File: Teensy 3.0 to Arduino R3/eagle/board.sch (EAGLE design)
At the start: 28 parts, among them IC1 7805TV

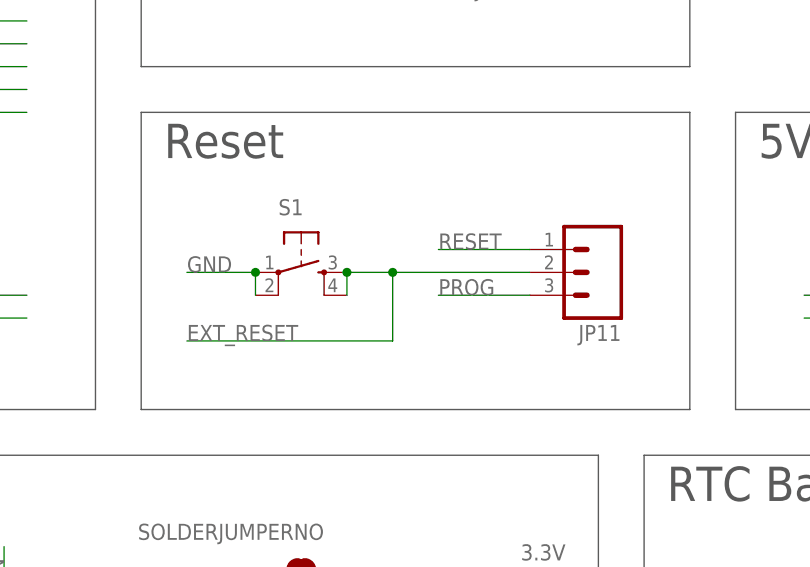
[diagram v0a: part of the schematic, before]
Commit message: update Arduino R3 board
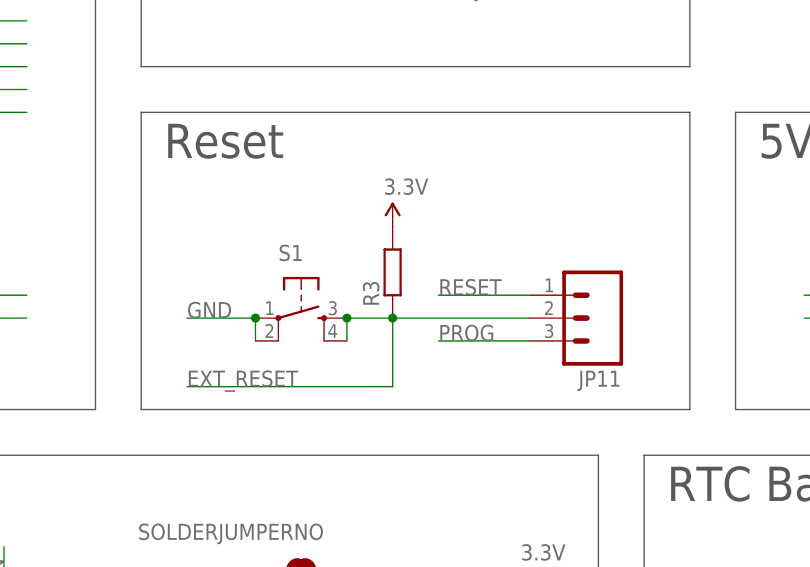
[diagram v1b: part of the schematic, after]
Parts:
- added R3: (no value), rcl:R-EU_R0805
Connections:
- net 3V3: now also R3.2
- net EXT_RESET: now also R3.1
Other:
- moved on the sheet: JP11, S1
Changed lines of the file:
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@@
 <part name="JP13" library="adafruit" deviceset="PINHD-1X13" device="_BIG"/>
 <part name="JP14" library="SparkFun-Connectors" deviceset="M02" device="PTH"/>
+<part name="R3" library="rcl" deviceset="R-EU_" device="R0805"/>
+<part name="P+3" library="SparkFun-Aesthetics" deviceset="3.3V" device=""/>
 </parts>
 <sheets>
@@
 <instance part="P+4" gate="G$1" x="203.2" y="60.96"/>
 <instance part="JP10" gate="G$1" x="147.32" y="40.64" rot="R90"/>
-<instance part="S1" gate="S" x="177.8" y="96.52"/>
+<instance part="S1" gate="S" x="177.8" y="91.44"/>
 <instance part="BAT1" gate="G$1" x="238.76" y="48.26"/>
-<instance part="JP11" gate="G$1" x="210.82" y="96.52" rot="R180"/>
+<instance part="JP11" gate="G$1" x="210.82" y="91.44" rot="R180"/>
 <instance part="JP12" gate="A" x="185.42" y="147.32"/>
 <instance part="JP13" gate="A" x="195.58" y="147.32" rot="R180"/>
 <instance part="JP14" gate="G$1" x="251.46" y="93.98" rot="R180"/>
+<instance part="R3" gate="G$1" x="187.96" y="96.52" rot="R90"/>
+<instance part="P+3" gate="G$1" x="187.96" y="101.6"/>
 </instances>
 <busses>
@@
 </segment>
 <segment>
-<wire x1="172.72" y1="96.52" x2="172.72" y2="93.98" width="0.1524" layer="91"/>
-<wire x1="172.72" y1="96.52" x2="165.1" y2="96.52" width="0.1524" layer="91"/>
-<label x="165.1" y="96.52" size="1.778" layer="95"/>
+<wire x1="172.72" y1="91.44" x2="172.72" y2="88.9" width="0.1524" layer="91"/>
+<wire x1="172.72" y1="91.44" x2="165.1" y2="91.44" width="0.1524" layer="91"/>
+<label x="165.1" y="91.44" size="1.778" layer="95"/>
 <pinref part="S1" gate="S" pin="1"/>
-<junction x="172.72" y="96.52"/>
+<junction x="172.72" y="91.44"/>
 <pinref part="S1" gate="S" pin="2"/>
 </segment>
@@
 <label x="236.22" y="93.98" size="1.778" layer="95"/>
 </segment>
+<segment>
+<pinref part="R3" gate="G$1" pin="2"/>
+<pinref part="P+3" gate="G$1" pin="3.3V"/>
+</segment>
 </net>
 <net name="A9" class="0">
@@
 <segment>
 <pinref part="JP11" gate="G$1" pin="3"/>
-<wire x1="203.2" y1="93.98" x2="193.04" y2="93.98" width="0.1524" layer="91"/>
-<label x="193.04" y="93.98" size="1.778" layer="95"/>
+<wire x1="203.2" y1="88.9" x2="193.04" y2="88.9" width="0.1524" layer="91"/>
+<label x="193.04" y="88.9" size="1.778" layer="95"/>
 </segment>
 </net>
@@
 <segment>
 <pinref part="JP11" gate="G$1" pin="1"/>
-<wire x1="203.2" y1="99.06" x2="193.04" y2="99.06" width="0.1524" layer="91"/>
-<label x="193.04" y="99.06" size="1.778" layer="95"/>
+<wire x1="203.2" y1="93.98" x2="193.04" y2="93.98" width="0.1524" layer="91"/>
+<label x="193.04" y="93.98" size="1.778" layer="95"/>
 </segment>
 </net>
@@
 </segment>
 <segment>
-<wire x1="182.88" y1="96.52" x2="182.88" y2="93.98" width="0.1524" layer="91"/>
-<wire x1="182.88" y1="96.52" x2="187.96" y2="96.52" width="0.1524" layer="91"/>
+<wire x1="182.88" y1="91.44" x2="182.88" y2="88.9" width="0.1524" layer="91"/>
+<wire x1="182.88" y1="91.44" x2="187.96" y2="91.44" width="0.1524" layer="91"/>
 <pinref part="S1" gate="S" pin="3"/>
-<junction x="182.88" y="96.52"/>
+<junction x="182.88" y="91.44"/>
 <pinref part="S1" gate="S" pin="4"/>
 <pinref part="JP11" gate="G$1" pin="2"/>
-<wire x1="187.96" y1="96.52" x2="203.2" y2="96.52" width="0.1524" layer="91"/>
-<wire x1="165.1" y1="88.9" x2="187.96" y2="88.9" width="0.1524" layer="91"/>
-<wire x1="187.96" y1="88.9" x2="187.96" y2="96.52" width="0.1524" layer="91"/>
-<junction x="187.96" y="96.52"/>
-<label x="165.1" y="88.9" size="1.778" layer="95"/>
-</segment>
-</net>
+<wire x1="187.96" y1="91.44" x2="203.2" y2="91.44" width="0.1524" layer="91"/>
+<wire x1="165.1" y1="83.82" x2="187.96" y2="83.82" width="0.1524" layer="91"/>
+<wire x1="187.96" y1="83.82" x2="187.96" y2="91.44" width="0.1524" layer="91"/>
+<junction x="187.96" y="91.44"/>
+<label x="165.1" y="83.82" size="1.778" layer="95"/>
+<pinref part="R3" gate="G$1" pin="1"/>
+</segment>
+</net>

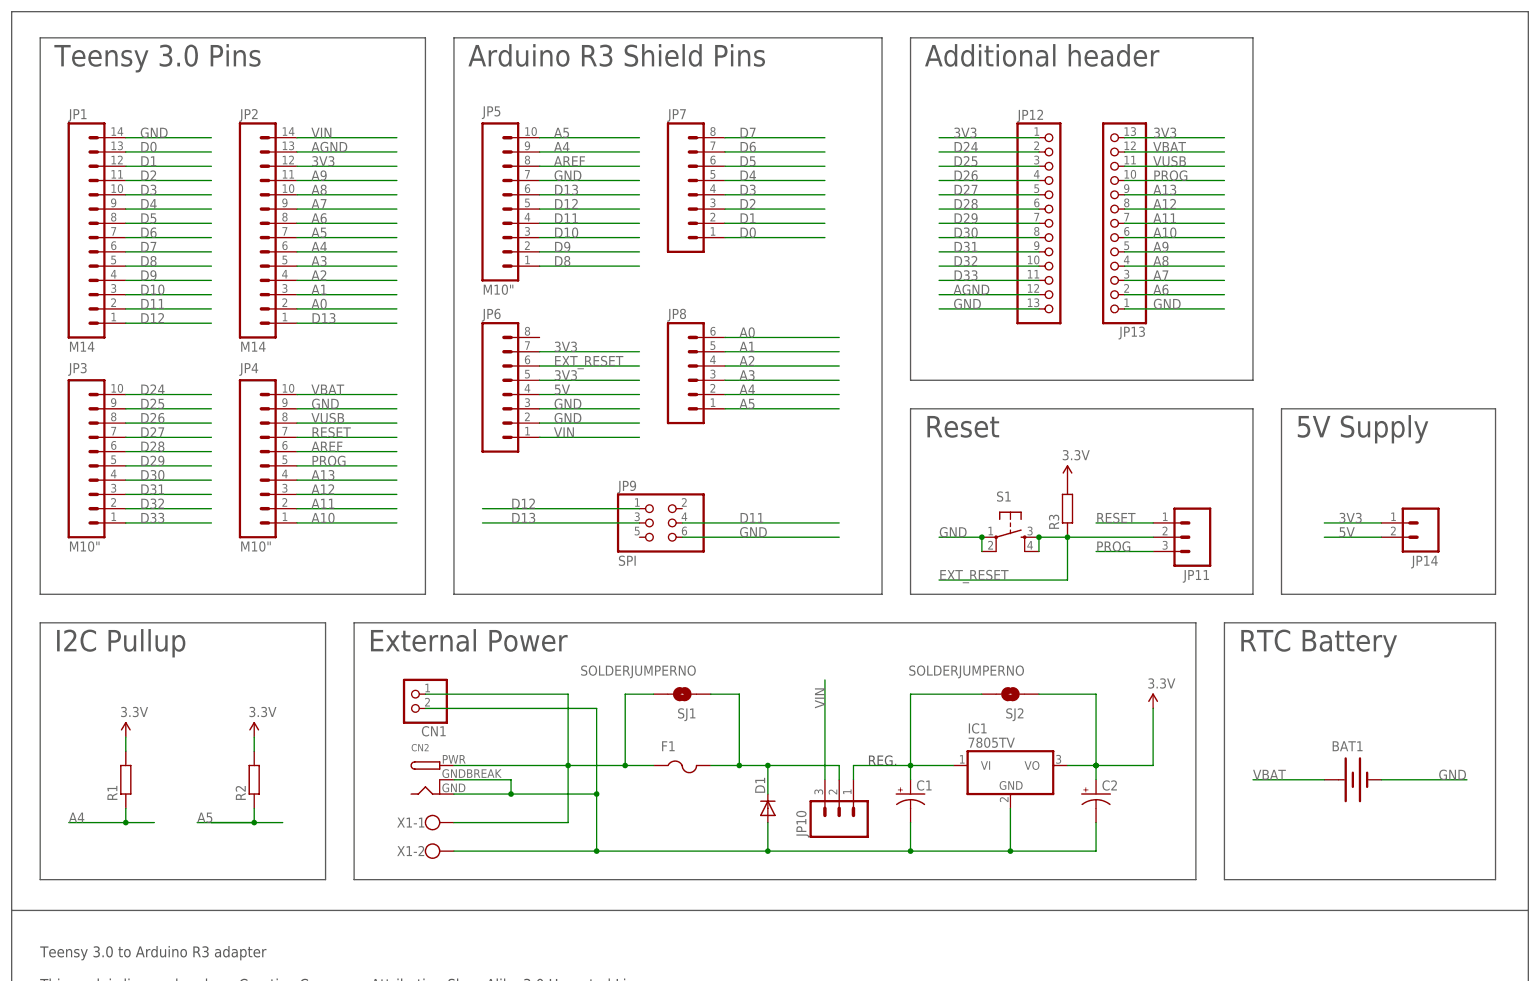
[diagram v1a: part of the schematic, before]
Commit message: update: -Arduino R3 pcb - breadboard pcb
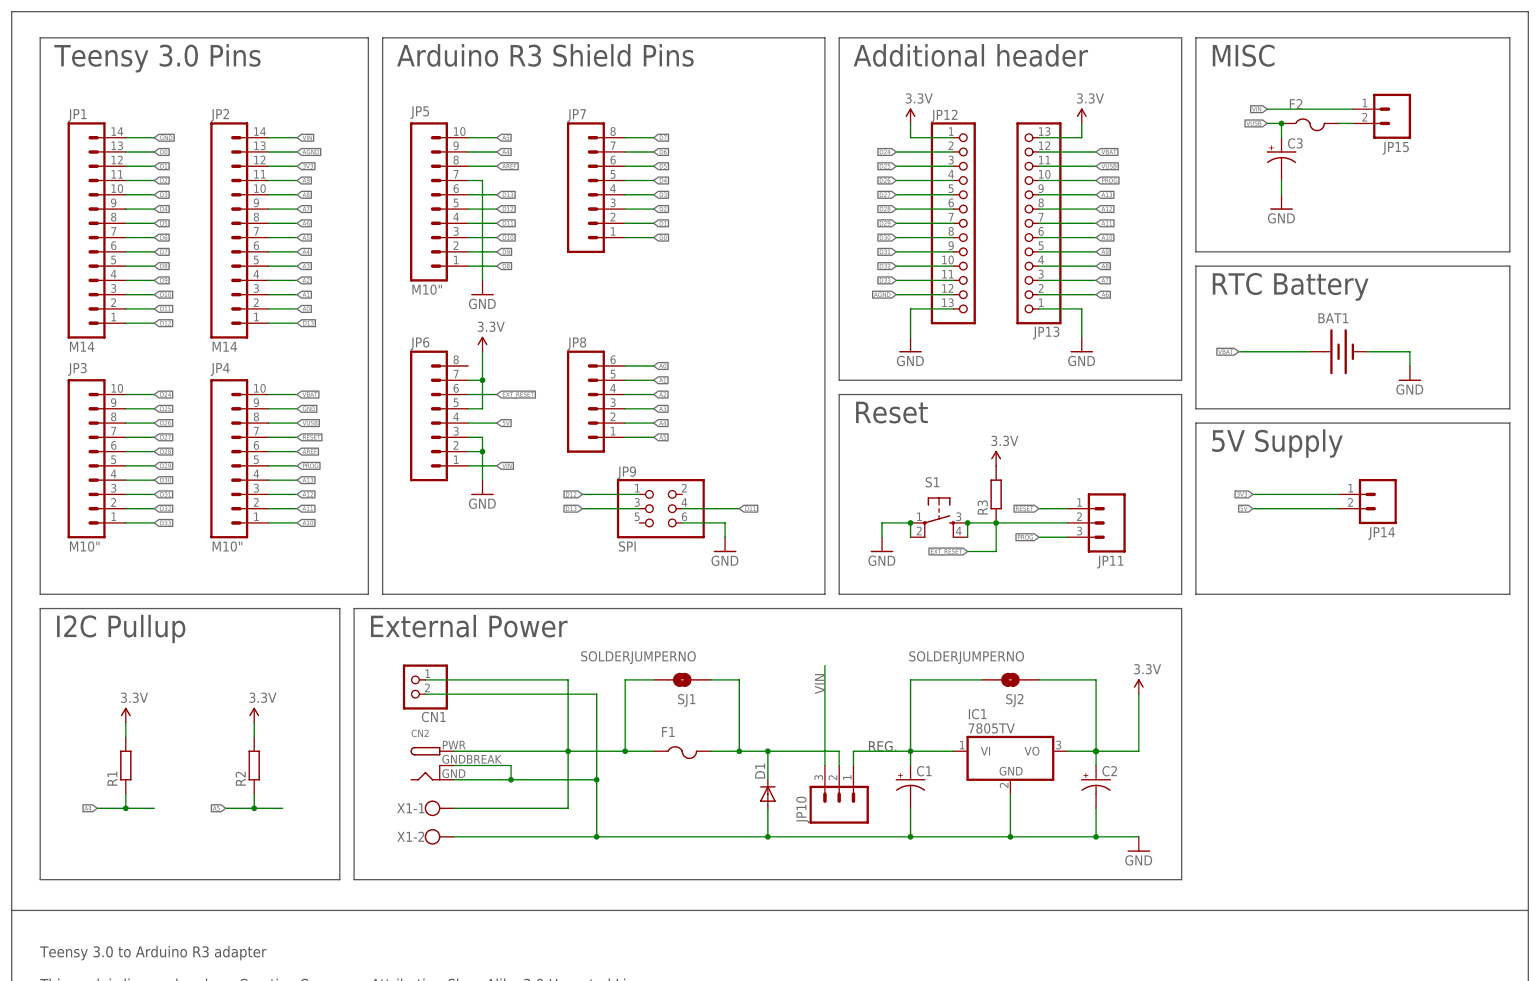
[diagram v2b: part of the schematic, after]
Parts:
- added C3: (no value), SparkFun-Capacitors:CAP_POL3528-KIT
- added F2: (no value), adafruit:PTCFUSE-1812
- added JP15: (no value), SparkFun-Connectors:M02PTH
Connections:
- new net N$2: F2.2, JP15.2
- net GND: now also C3.-
- net VIN: now also JP15.1
- net VUSB: now also C3.+, F2.1
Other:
- note added: "MISC"
- moved on the sheet: BAT1, C1, C2, CN1, CN2, D1, F1, IC1, JP10, JP11, JP12, JP13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

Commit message: added i2c eeprom, sdcard
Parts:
- added C4, C5, C6, C7, C8: (no value), rcl:C-EUC0805K
- added IC2, IC3, IC4, IC5: 24AA256SN, microchip:24AA256SN
- added R4: (no value), resistor:R-EU_R0805
- added U1: MICROSD, adafruit:MICROSD
- BAT1: device SparkFun-Electromechanical:BATTERY12PTH -> SparkFun-Electromechanical:BATTERY12MM
- C1, C2: device SparkFun-Capacitors:CAP_POL3528-KIT -> resistor:CPOL-EUCT3216
- R1, R2, R3: device rcl:R-EU_R0805 -> resistor:R-EU_R0805
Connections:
- new net 3.3V: JP2.12
- net 3V3: now also C4.1, C5.1, C6.1, C7.1, C8.1, IC2.A2, IC2.VCC, IC3.A1, IC3.A2, IC3.VCC, IC4.A0, IC4.A2, IC4.VCC, IC5.A0, IC5.A1, IC5.A2, IC5.VCC, R4.2, U1.VDD; no longer JP2.12
- net A4: now also IC2.SDA, IC3.SDA, IC4.SDA, IC5.SDA
- net A5: now also IC2.SCL, IC3.SCL, IC4.SCL, IC5.SCL
- net D10: now also U1.CS
- net D11: now also U1.DATA_IN
- net D12: now also U1.DATA_OUT
- net D13: now also U1.SCLK
- net D8: now also R4.1, U1.CARD_DETECT
- net GND: now also C4.2, C5.2, C6.2, C7.2, C8.2, IC2.A0, IC2.A1, IC2.GND, IC2.WP, IC3.A0, IC3.GND, IC3.WP, IC4.A1, IC4.GND, IC4.WP, IC5.GND, IC5.WP, U1.GND, U1.GND1, U1.VSS
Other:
- note added: "I2C EEPROM"
- note added: "uSD socket"
- moved on the sheet: JP3, JP4

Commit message: Version 3 final
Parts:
- added C9: (no value), resistor:CPOL-EUD
- added D2: (no value), SparkFun-DiscreteSemi:DIODESMA-KIT
- added R10, R11, R12, R13, R14, R15, R16, R17, R18, R19, R20, R21, R22, R23, R24, R5, R6, R7, R8, R9: (no value), resistor:R-EU_R0805
- added SJ3, SJ4, SJ5, SJ6: SOLDERJUMPERNO, SparkFun-Passives:SOLDERJUMPERNO
- IC1: value 7805TV -> 78XX compatible
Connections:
- removed net 3V3: C2.+, C4.1, C5.1, C6.1, C7.1, C8.1, IC1.VO, IC2.A2, IC2.VCC, IC3.A1, IC3.A2, IC3.VCC, IC4.A0, IC4.A2, IC4.VCC, IC5.A0, IC5.A1, IC5.A2, IC5.VCC, JP12.1, JP13.13, JP14.1, JP6.5, JP6.7, R1.2, R2.2, R3.2, R4.2, SJ2.1, U1.VDD
- new net N$10: JP2.7, R10.2
- new net N$11: JP2.6, R11.2
- new net N$12: JP2.5, R12.2
- new net N$13: JP1.13, R13.2
- new net N$14: JP1.12, R14.2
- new net N$15: JP1.11, R15.2
- new net N$16: JP1.10, R16.2
- new net N$17: JP1.9, R17.2
- new net N$18: JP1.8, R18.2
- new net N$19: JP1.7, R19.2
- new net N$20: JP1.6, R20.2
- new net N$21: JP2.4, R21.2
- new net N$22: JP2.3, R22.2
- new net N$23: JP2.2, R23.2
- new net N$24: JP2.1, R24.2
- new net N$5: JP1.5, R5.2
- new net N$6: JP1.4, R6.2
- new net N$7: JP1.3, R7.2
- new net N$8: JP1.2, R8.2
- new net N$9: JP1.1, R9.2
- new net NIC: R4.1, SJ3.1, SJ4.1, U1.CARD_DETECT
- new net QW: SJ5.1, SJ6.1, U1.CS
- net 3.3V: now also C2.+, C4.1, C5.1, C6.1, C7.1, C8.1, C9.+, D2.A, IC1.VO, IC2.A2, IC2.VCC, IC3.A1, IC3.A2, IC3.VCC, IC4.A0, IC4.A2, IC4.VCC, IC5.A0, IC5.A1, IC5.A2, IC5.VCC, JP12.1, JP13.13, JP14.1, JP6.5, JP6.7, R1.2, R2.2, R3.2, R4.2, SJ2.1, U1.VDD
- net A0: now also R23.1; no longer JP2.2
- net A1: now also R22.1; no longer JP2.3
- net A2: now also R21.1; no longer JP2.4
- net A3: now also R12.1; no longer JP2.5
- net A4: now also R11.1; no longer JP2.6
- net A5: now also R10.1; no longer JP2.7
- net D0: now also R13.1; no longer JP1.13
- net D1: now also R14.1; no longer JP1.12
- net D10: now also R7.1, SJ6.2; no longer JP1.3, U1.CS
- net D11: now also R8.1; no longer JP1.2
- net D12: now also R9.1; no longer JP1.1
- net D13: now also R24.1; no longer JP2.1
- net D2: now also R15.1; no longer JP1.11
- net D3: now also R16.1; no longer JP1.10
- net D4: now also R17.1; no longer JP1.9
- net D5: now also R18.1; no longer JP1.8
- net D6: now also R19.1; no longer JP1.7
- net D7: now also R20.1, SJ3.2; no longer JP1.6
- net D8: now also R5.1, SJ4.2; no longer JP1.5, R4.1, U1.CARD_DETECT
- net D9: now also R6.1, SJ5.2; no longer JP1.4
- net GND: now also C9.-
- net N$3: now also D2.C
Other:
- moved on the sheet: BAT1, C3, C4, F2, JP1, JP11, JP12, JP13, JP14, JP15, JP2, JP3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

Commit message: V3-2: fixed several bugs
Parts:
- added C10: (no value), rcl:CPOL-EUSANYO_SMD_E7
- added JP16: (no value), SparkFun-Connectors:M02PTH
- C3: device SparkFun-Capacitors:CAP_POL3528-KIT -> rcl:CPOL-EUA/3216-18W
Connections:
- new net N$25: C10.+, JP16.2
- net GND: now also C10.-
- net N$2: now also JP16.1
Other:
- moved on the sheet: C3, F2, JP15
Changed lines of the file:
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@@
 <part name="F2" library="adafruit" deviceset="PTCFUSE" device="-1812"/>
 <part name="JP15" library="SparkFun-Connectors" deviceset="M02" device="PTH"/>
-<part name="C3" library="SparkFun-Capacitors" deviceset="CAP_POL" device="3528-KIT"/>
+<part name="C3" library="rcl" deviceset="CPOL-EU" device="A/3216-18W"/>
 <part name="GND1" library="SparkFun-Aesthetics" deviceset="GND" device=""/>
 <part name="GND2" library="SparkFun-Aesthetics" deviceset="GND" device=""/>
@@
 <part name="R23" library="resistor" deviceset="R-EU_" device="R0805"/>
 <part name="R24" library="resistor" deviceset="R-EU_" device="R0805"/>
+<part name="GND22" library="SparkFun-Aesthetics" deviceset="GND" device=""/>
+<part name="JP16" library="SparkFun-Connectors" deviceset="M02" device="PTH"/>
+<part name="C10" library="rcl" deviceset="CPOL-EU" device="SANYO_SMD_E7"/>
 </parts>
 <sheets>
@@
 <instance part="R3" gate="G$1" x="198.12" y="99.06" rot="R90"/>
 <instance part="P+3" gate="G$1" x="198.12" y="104.14"/>
-<instance part="F2" gate="G$1" x="393.7" y="99.06"/>
-<instance part="JP15" gate="G$1" x="408.94" y="104.14" rot="R180"/>
-<instance part="C3" gate="G$1" x="388.62" y="96.52"/>
-<instance part="GND1" gate="1" x="388.62" y="86.36"/>
+<instance part="F2" gate="G$1" x="391.16" y="102.87"/>
+<instance part="JP15" gate="G$1" x="415.29" y="107.95" rot="R180"/>
+<instance part="C3" gate="G$1" x="386.08" y="97.79"/>
+<instance part="GND1" gate="1" x="386.08" y="82.55"/>
 <instance part="GND2" gate="1" x="106.68" y="99.06"/>
 <instance part="GND3" gate="1" x="149.86" y="88.9"/>
@@
 <attribute name="VALUE" x="72.39" y="134.112" size="1.778" layer="96" rot="R180"/>
 </instance>
+<instance part="GND22" gate="1" x="401.32" y="82.55"/>
+<instance part="JP16" gate="G$1" x="415.29" y="95.25" rot="R180"/>
+<instance part="C10" gate="G$1" x="401.32" y="90.17"/>
 </instances>
 <busses>
@@
 <pinref part="C3" gate="G$1" pin="-"/>
 <pinref part="GND1" gate="1" pin="GND"/>
-<wire x1="388.62" y1="91.44" x2="388.62" y2="88.9" width="0.1524" layer="91"/>
+<wire x1="386.08" y1="92.71" x2="386.08" y2="85.09" width="0.1524" layer="91"/>
 </segment>
 <segment>
@@
 <wire x1="457.2" y1="147.32" x2="459.74" y2="147.32" width="0.1524" layer="91"/>
 </segment>
+<segment>
+<pinref part="GND22" gate="1" pin="GND"/>
+<pinref part="C10" gate="G$1" pin="-"/>
+</segment>
 </net>
 <net name="D0" class="0">
@@
 <segment>
 <pinref part="JP15" gate="G$1" pin="1"/>
-<wire x1="401.32" y1="104.14" x2="386.08" y2="104.14" width="0.1524" layer="91"/>
-<label x="386.08" y="104.14" size="0.8128" layer="95" rot="R180" xref="yes"/>
+<wire x1="407.67" y1="107.95" x2="383.54" y2="107.95" width="0.1524" layer="91"/>
+<label x="383.54" y="107.95" size="0.8128" layer="95" rot="R180" xref="yes"/>
 </segment>
 </net>
@@
 <segment>
 <pinref part="F2" gate="G$1" pin="1"/>
-<wire x1="388.62" y1="101.6" x2="386.08" y2="101.6" width="0.1524" layer="91"/>
-<label x="386.08" y="101.6" size="0.8128" layer="95" rot="R180" xref="yes"/>
+<wire x1="386.08" y1="105.41" x2="383.54" y2="105.41" width="0.1524" layer="91"/>
+<label x="383.54" y="105.41" size="0.8128" layer="95" rot="R180" xref="yes"/>
 <pinref part="C3" gate="G$1" pin="+"/>
-<wire x1="388.62" y1="99.06" x2="388.62" y2="101.6" width="0.1524" layer="91"/>
-<junction x="388.62" y="101.6"/>
+<wire x1="386.08" y1="100.33" x2="386.08" y2="105.41" width="0.1524" layer="91"/>
+<junction x="386.08" y="105.41"/>
 </segment>
 </net>
@@
 <pinref part="F2" gate="G$1" pin="2"/>
 <pinref part="JP15" gate="G$1" pin="2"/>
-<wire x1="398.78" y1="101.6" x2="401.32" y2="101.6" width="0.1524" layer="91"/>
+<wire x1="396.24" y1="105.41" x2="401.32" y2="105.41" width="0.1524" layer="91"/>
+<pinref part="JP16" gate="G$1" pin="1"/>
+<wire x1="401.32" y1="105.41" x2="407.67" y2="105.41" width="0.1524" layer="91"/>
+<wire x1="407.67" y1="95.25" x2="401.32" y2="95.25" width="0.1524" layer="91"/>
+<wire x1="401.32" y1="95.25" x2="401.32" y2="105.41" width="0.1524" layer="91"/>
+<junction x="401.32" y="105.41"/>
 </segment>
 </net>
@@
 </segment>
 </net>
+<net name="N$25" class="0">
+<segment>
+<pinref part="C10" gate="G$1" pin="+"/>
+<pinref part="JP16" gate="G$1" pin="2"/>
+<wire x1="401.32" y1="92.71" x2="407.67" y2="92.71" width="0.1524" layer="91"/>
+</segment>
+</net>
